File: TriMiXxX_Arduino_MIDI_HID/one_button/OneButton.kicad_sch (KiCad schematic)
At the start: 18 parts, among them J1 INPUT, J2 OUTPUT, SW1 TS-1187A-B-A-B, U1 CH32V003F4U6

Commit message: Revise onebutton board for future DMA instead of bitbanging, and add test and firmware
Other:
- note added: "PC6 is SPI MOSI, which allow DMA and helps us avoid bit-banging the LED with the CPU. FOR V2: Switch the LED to PC6!!"
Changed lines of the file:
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@@
 	(generator_version "10.0")
 	(paper "A4")
+	(text "PC6 is SPI MOSI, which \nallow DMA and helps us \navoid bit-banging the LED \nwith the CPU.\n\nFOR V2: Switch the LED to PC6!!"
+		(exclude_from_sim no)
+		(at 194.31 104.394 0)
+		(effects
+			(font
+				(size 1 1)
+			)
+			(justify left)
+		)
+	)
 	(junction
 		(at 151.13 102.87)

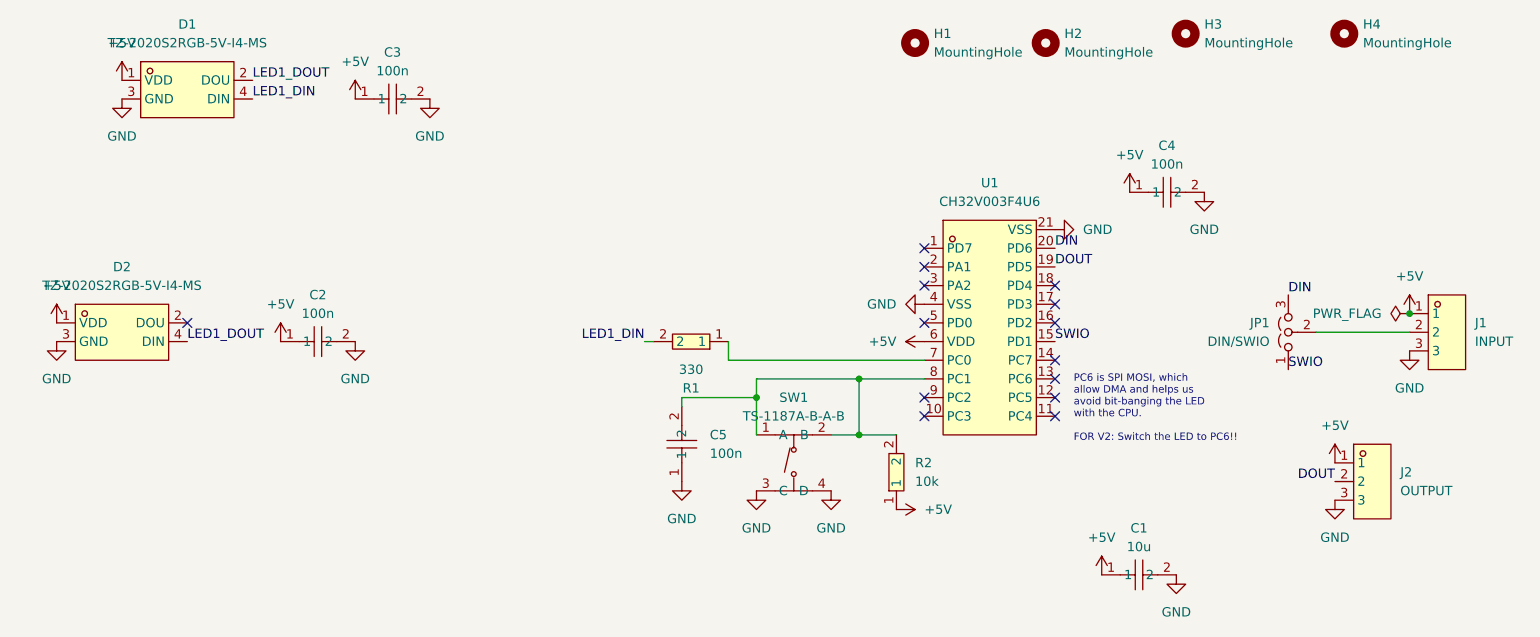
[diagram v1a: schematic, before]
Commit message: Init trimixxx-midi platformIO project
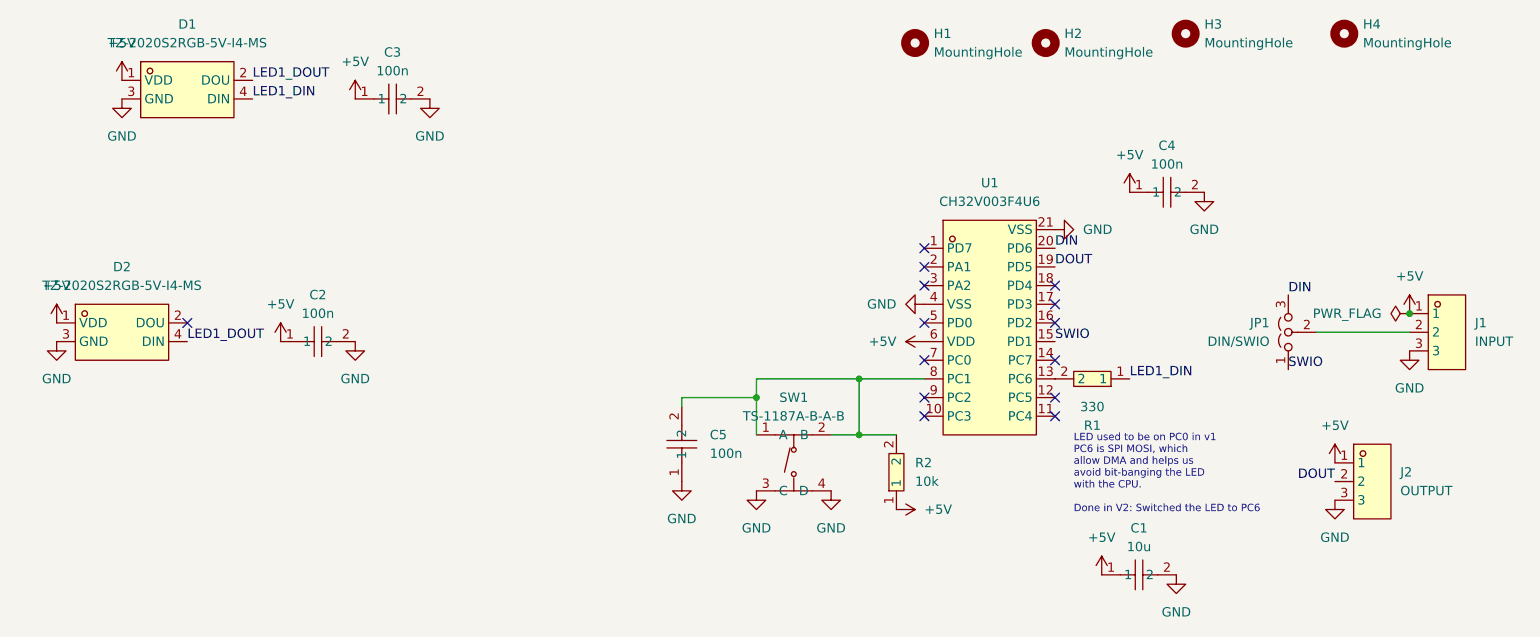
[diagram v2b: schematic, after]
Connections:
- net LED1_DIN: now also R1.1; no longer R1.2
- net at U1.7 (PC0): no longer R1.1
- net at U1.13 (PC6): now also R1.2
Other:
- note added: "LED used to be on PC0 in v1 PC6 is SPI MOSI, which allow DMA and helps us avoid bit-banging the LED with the CPU. Done in V2: Switched the LED to PC6"
- note removed: "PC6 is SPI MOSI, which allow DMA and helps us avoid bit-banging the LED with the CPU. FOR V2: Switch the LED to PC6!!"
- title: (none) -> OneButton board
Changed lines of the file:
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@@
 	(generator_version "10.0")
 	(paper "A4")
-	(text "PC6 is SPI MOSI, which \nallow DMA and helps us \navoid bit-banging the LED \nwith the CPU.\n\nFOR V2: Switch the LED to PC6!!"
-		(exclude_from_sim no)
-		(at 194.31 104.394 0)
+	(title_block
+		(title "OneButton board")
+		(rev "v2")
+		(comment 1 "V2: Switched LED from PC0 to PC6 to allow DMA through PC6 SPI MOSI capability")
+	)
+	(text "LED used to be on PC0 in v1\nPC6 is SPI MOSI, which \nallow DMA and helps us \navoid bit-banging the LED \nwith the CPU.\n\nDone in V2: Switched the LED to PC6"
+		(exclude_from_sim no)
+		(at 194.31 113.284 0)
 		(effects
 			(font
@@
 	)
 	(no_connect
+		(at 173.99 97.79)
+	)
+	(no_connect
 		(at 191.77 97.79)
 	)
@@
 	(no_connect
 		(at 173.99 87.63)
-	)
-	(no_connect
-		(at 191.77 100.33)
 	)
 	(no_connect
@@
 	(wire
 		(pts
-			(xy 135.89 95.25) (xy 137.16 95.25)
+			(xy 170.18 107.95) (xy 165.1 107.95)
 		)
 		(stroke
@@
 	(wire
 		(pts
-			(xy 170.18 107.95) (xy 165.1 107.95)
+			(xy 165.1 100.33) (xy 151.13 100.33)
 		)
 		(stroke
@@
 	(wire
 		(pts
-			(xy 165.1 100.33) (xy 151.13 100.33)
+			(xy 227.33 93.98) (xy 240.03 93.98)
 		)
 		(stroke
@@
 	(wire
 		(pts
-			(xy 227.33 93.98) (xy 240.03 93.98)
+			(xy 165.1 107.95) (xy 165.1 100.33)
 		)
 		(stroke
@@
 	(wire
 		(pts
-			(xy 165.1 107.95) (xy 165.1 100.33)
+			(xy 151.13 102.87) (xy 151.13 107.95)
 		)
 		(stroke
@@
 	(wire
 		(pts
-			(xy 151.13 102.87) (xy 151.13 107.95)
+			(xy 140.97 102.87) (xy 140.97 104.14)
 		)
 		(stroke
@@
 	(wire
 		(pts
-			(xy 140.97 102.87) (xy 140.97 104.14)
-		)
-		(stroke
-			(width 0)
-			(type default)
-		)
-	)
-	(wire
-		(pts
 			(xy 161.29 107.95) (xy 165.1 107.95)
-		)
-		(stroke
-			(width 0)
-			(type default)
-		)
-	)
-	(wire
-		(pts
-			(xy 147.32 97.79) (xy 147.32 95.25)
-		)
-		(stroke
-			(width 0)
-			(type default)
-		)
-	)
-	(wire
-		(pts
-			(xy 173.99 97.79) (xy 147.32 97.79)
 		)
 		(stroke
@@
 		)
 	)
-	(label "LED1_DIN"
-		(at 135.89 95.25 180)
-		(effects
-			(font
-				(size 1.27 1.27)
-			)
-			(justify right bottom)
-		)
-	)
 	(label "SWIO"
 		(at 223.52 99.06 0)
@@
 	(label "DOUT"
 		(at 191.77 85.09 0)
+		(effects
+			(font
+				(size 1.27 1.27)
+			)
+			(justify left bottom)
+		)
+	)
+	(label "LED1_DIN"
+		(at 201.93 100.33 0)
 		(effects
 			(font
@@
 	)
 	(symbol
+		(lib_id "easyeda2kicad:0603WAF3300T5E")
+		(at 196.85 100.33 180)
+		(unit 1)
+		(body_style 1)
+		(exclude_from_sim no)
+		(in_bom yes)
+		(on_board yes)
+		(in_pos_files yes)
+		(dnp no)
+		(fields_autoplaced yes)
+		(property "Reference" "R1"
+			(at 196.85 106.68 0)
+			(show_name no)
+			(do_not_autoplace no)
+			(effects
+				(font
+					(size 1.27 1.27)
+				)
+			)
+		)
+		(property "Value" "330"
+			(at 196.85 104.14 0)
+			(show_name no)
+			(do_not_autoplace no)
+			(effects
+				(font
+					(size 1.27 1.27)
+				)
+			)
+		)
+		(property "Footprint" "easyeda2kicad:R0603"
+			(at 196.85 92.71 0)
+			(hide yes)
+			(show_name no)
+			(do_not_autoplace no)
+			(effects
+				(font
+					(size 1.27 1.27)
+				)
+			)
+		)
+		(property "Datasheet" "https://lcsc.com/product-detail/Chip-Resistor-Surface-Mount-UniOhm_330R-3300-1_C23138.html"
+			(at 196.85 90.17 0)
+			(hide yes)
+			(show_name no)
+			(do_not_autoplace no)
+			(effects
+				(font
+					(size 1.27 1.27)
+				)
+			)
+		)
+		(property "Description" "330Ω (3300) ±1%"
+			(at 196.85 100.33 0)
+			(hide yes)
+			(show_name no)
+			(do_not_autoplace no)
+			(effects
+				(font
+					(size 1.27 1.27)
+				)
+			)
+		)
+		(property "Manufacturer" "UNI-ROYAL(厚声)"
+			(at 196.85 87.63 0)
+			(hide yes)
+			(show_name no)
+			(do_not_autoplace no)
+			(effects
+				(font
+					(size 1.27 1.27)
+				)
+			)
+		)
+		(property "MPN" "0603WAF3300T5E"
+			(at 196.85 85.09 0)
+			(hide yes)
+			(show_name no)
+			(do_not_autoplace no)
+			(effects
+				(font
+					(size 1.27 1.27)
+				)
+			)
+		)
+		(property "LCSC Part" "C23138"
+			(at 196.85 82.55 0)
+			(hide yes)
+			(show_name no)
+			(do_not_autoplace no)
+			(effects
+				(font
+					(size 1.27 1.27)
+				)
+			)
+		)
+		(pin "2"
+		)
+		(pin "1"
+		)
+		(instances
+			(project "OneButton"
+				(path "/d1fdf717-1f9c-48a0-97b7-d2ea3a3c6742"
+					(reference "R1")
+					(unit 1)
+				)
+			)
+		)
+	)
+	(symbol
 		(lib_id "Mechanical:MountingHole")
 		(at 190.5 54.61 0)
@@
 					(unit 1)
 				)
-			)
-		)
-	)
-	(symbol
-		(lib_id "easyeda2kicad:0603WAF3300T5E")
-		(at 142.24 95.25 180)
-		(unit 1)
-		(body_style 1)
-		(exclude_from_sim no)
-		(in_bom yes)
-		(on_board yes)
-		(in_pos_files yes)
-		(dnp no)
-		(fields_autoplaced yes)
-		(property "Reference" "R1"
-			(at 142.24 101.6 0)
-			(show_name no)
-			(do_not_autoplace no)
-			(effects
-				(font
-					(size 1.27 1.27)
-				)
-			)
-		)
-		(property "Value" "330"
-			(at 142.24 99.06 0)
-			(show_name no)
-			(do_not_autoplace no)
-			(effects
-				(font
-					(size 1.27 1.27)
-				)
-			)
-		)
-		(property "Footprint" "easyeda2kicad:R0603"
-			(at 142.24 87.63 0)
-			(hide yes)
-			(show_name no)
-			(do_not_autoplace no)
-			(effects
-				(font
-					(size 1.27 1.27)
-				)
-			)
-		)
-		(property "Datasheet" "https://lcsc.com/product-detail/Chip-Resistor-Surface-Mount-UniOhm_330R-3300-1_C23138.html"
-			(at 142.24 85.09 0)
-			(hide yes)
-			(show_name no)
-			(do_not_autoplace no)
-			(effects
-				(font
-					(size 1.27 1.27)
-				)
-			)
-		)
-		(property "Description" "330Ω (3300) ±1%"
-			(at 142.24 95.25 0)
-			(hide yes)
-			(show_name no)
-			(do_not_autoplace no)
-			(effects
-				(font
-					(size 1.27 1.27)
-				)
-			)
-		)
-		(property "Manufacturer" "UNI-ROYAL(厚声)"
-			(at 142.24 82.55 0)
-			(hide yes)
-			(show_name no)
-			(do_not_autoplace no)
-			(effects
-				(font
-					(size 1.27 1.27)
-				)
-			)
-		)
-		(property "MPN" "0603WAF3300T5E"
-			(at 142.24 80.01 0)
-			(hide yes)
-			(show_name no)
-			(do_not_autoplace no)
-			(effects
-				(font
-					(size 1.27 1.27)
-				)
-			)
-		)
-		(property "LCSC Part" "C23138"
-			(at 142.24 77.47 0)
-			(hide yes)
-			(show_name no)
-			(do_not_autoplace no)
-			(effects
-				(font
-					(size 1.27 1.27)
-				)
-			)
-		)
-		(pin "2"
-		)
-		(pin "1"
-		)
-		(instances
-			(project "OneButton"
-				(path "/d1fdf717-1f9c-48a0-97b7-d2ea3a3c6742"
-					(reference "R1")
-					(unit 1)
-				)
